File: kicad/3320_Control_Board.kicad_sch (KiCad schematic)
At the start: 8 parts, among them J1 Sig In, J2 Sig Out, J3 FreqCv, J4 ResCv

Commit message: updated pcb revision 0.1.0
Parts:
- added H1: MountingHole_Pad, DIYSynthMNL:MountingHole_M3_Standoff_Pad, symbol Mechanical:MountingHole_Pad
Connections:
- net CB_GND: now also H1.1
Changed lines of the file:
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@@
   (no_connect (at 127 66.04))
   (no_connect (at 205.74 66.04))
+  (wire (pts (xy 209.55 137.16) (xy 209.55 139.7))
+    (stroke (width 0) (type default))
+  )
   (wire (pts (xy 127 111.76) (xy 134.62 111.76))
     (stroke (width 0) (type default))
@@
   )
   (label "CB_+12V" (at 166.37 135.89 0) (fields_autoplaced)
+    (effects (font (size 1.27 1.27)) (justify left bottom))
+  )
+  (label "CB_GND" (at 209.55 139.7 0) (fields_autoplaced)
     (effects (font (size 1.27 1.27)) (justify left bottom))
   )
@@
         )
       )
+    )
+  )
+  (symbol (lib_id "Mechanical:MountingHole_Pad") (at 209.55 134.62 0) (unit 1)
+    (in_bom yes) (on_board yes) (dnp no) (fields_autoplaced)
+    (property "Reference" "H1" (at 212.09 132.08 0)
+      (effects (font (size 1.27 1.27)) (justify left))
+    )
+    (property "Value" "MountingHole_Pad" (at 212.09 134.62 0)
+      (effects (font (size 1.27 1.27)) (justify left))
+    )
+    (property "Footprint" "DIYSynthMNL:MountingHole_M3_Standoff_Pad" (at 209.55 134.62 0)
+      (effects (font (size 1.27 1.27)) hide)
+    )
+    (property "Datasheet" "~" (at 209.55 134.62 0)
+      (effects (font (size 1.27 1.27)) hide)
+    )
+    (pin "1")
+    (instances
+      (project "3320-VCF"
+        (path "/03f11930-f7c0-4ced-9742-79790ca3496b/6be4c3d1-05b5-4b24-bcf9-a639c6a20d54"
+          (reference "H1") (unit 1)
+        )
+        (path "/03f11930-f7c0-4ced-9742-79790ca3496b/dcf24f11-8609-4732-a8b1-622b67325503"
+          (reference "H2") (unit 1)
+        )
+      )

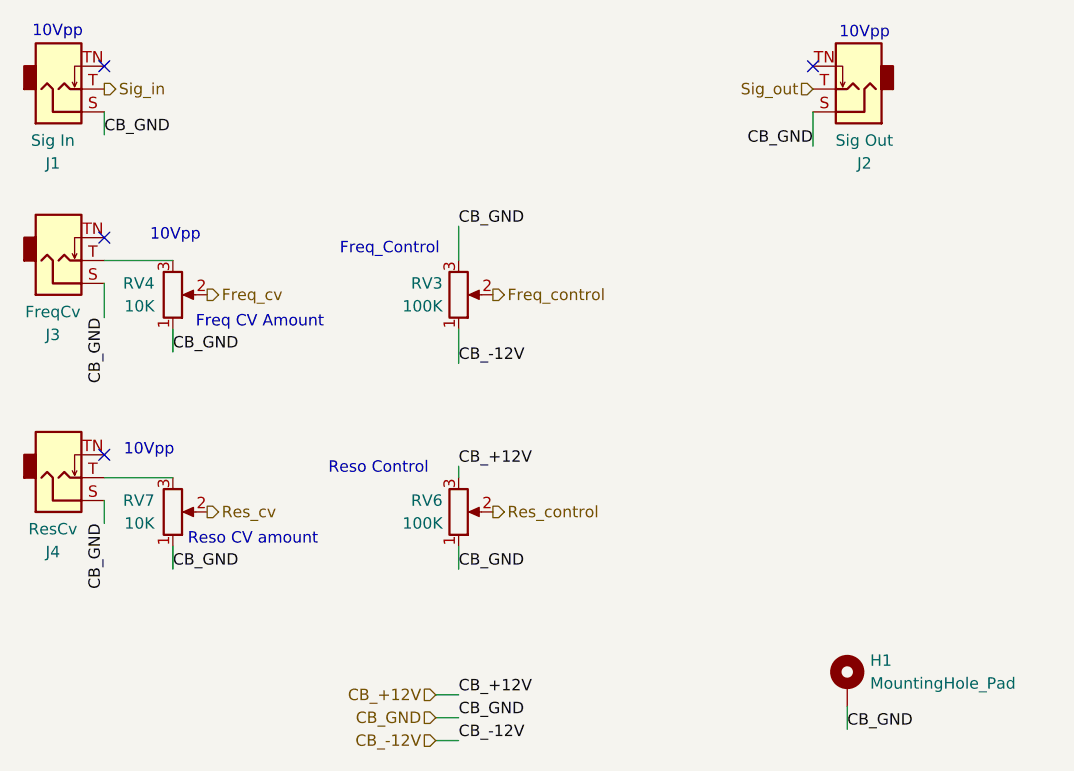
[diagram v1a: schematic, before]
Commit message: Add schematic revision 0.1.5
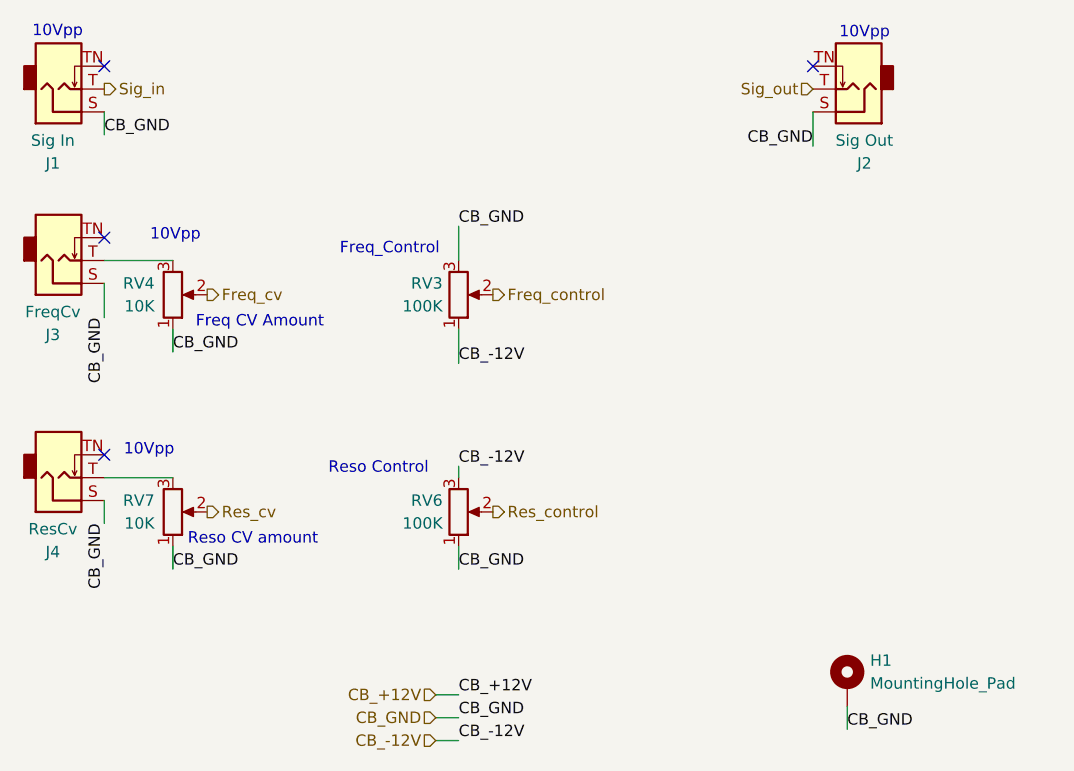
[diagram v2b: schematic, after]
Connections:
- net CB_+12V: no longer RV6.3
- net CB_-12V: now also RV6.3
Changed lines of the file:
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@@
     (title "Eurorack 3320 Low Pass VCF")
     (date "2024-02-16")
-    (rev "0.1.4")
+    (rev "0.1.5")
     (company "DIYSynthMNL")
     (comment 1 "This version is a prototype")
@@
     (effects (font (size 1.27 1.27)) (justify left bottom))
   )
+  (label "CB_-12V" (at 166.37 110.49 0) (fields_autoplaced)
+    (effects (font (size 1.27 1.27)) (justify left bottom))
+  )
   (label "CB_-12V" (at 166.37 140.97 0) (fields_autoplaced)
     (effects (font (size 1.27 1.27)) (justify left bottom))
@@
     (effects (font (size 1.27 1.27)) (justify left bottom))
   )
-  (label "CB_+12V" (at 166.37 110.49 0) (fields_autoplaced)
-    (effects (font (size 1.27 1.27)) (justify left bottom))
-  )
